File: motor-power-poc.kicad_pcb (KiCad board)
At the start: 4 copper layers, 70 x 50 mm, 159 parts, among them J1 Conn_01x04_Pin, J2 USB_C_Receptacle_USB2.0_14P, J3 Conn_01x02, J4 Conn_02x02_Counter_Clockwise, J5 Conn_02x06_Counter_Clockwise, M1 Motor_Servo, M2 Motor_Servo, M3 DC, Q1 Q_NMOS, Q10 Q_NMOS, Q2 Q_NMOS, Q3 Q_NMOS, Q4 Q_NMOS, Q5 Q_NMOS, Q6 Q_NMOS, Q7 Q_NMOS, Q8 Q_NMOS, Q9 Q_NMOS, SW1 SW_Push, SW2 SW_Push, U1 QRE1113GR, U10 CJ431, U11 DRV8701, U2 QRE1113GR, U3 QRE1113GR, U4 ESP32-S3FH4R2, U5 LM74502, U6 TPS5430DDA, U7 TPS56A37, U8 TPS2121, U9 LDL212PV33R, Y1 48M

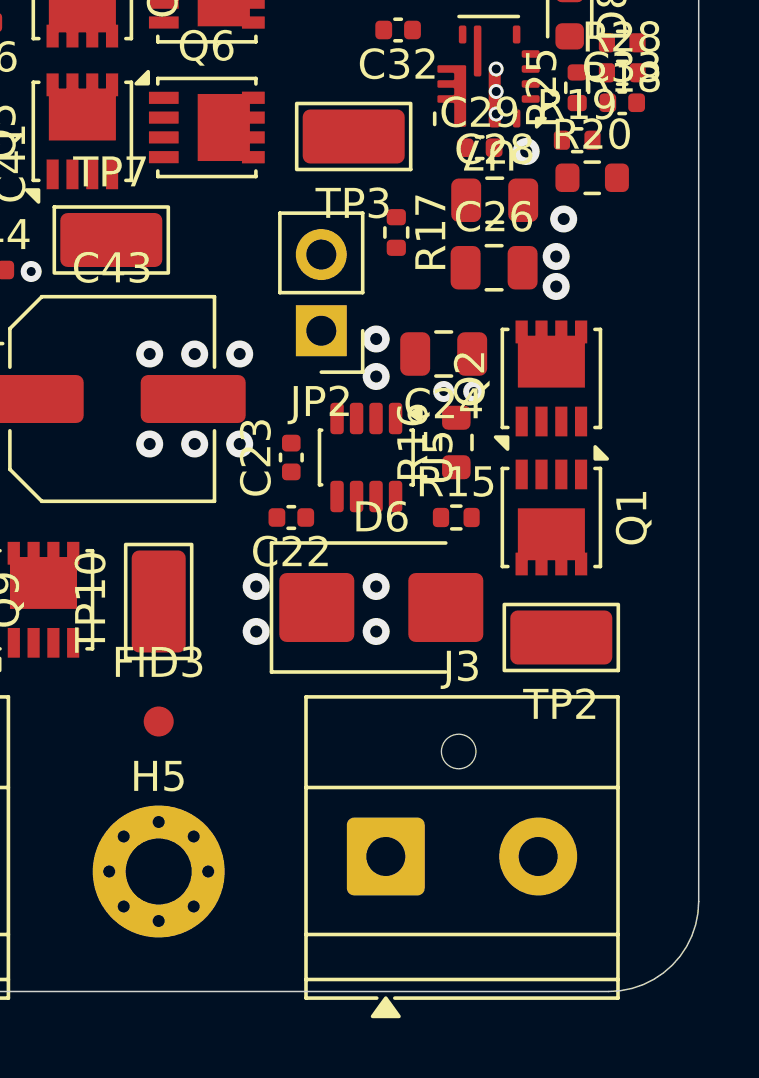
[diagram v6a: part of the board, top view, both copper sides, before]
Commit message: pcb: add LM74502H RPP routing
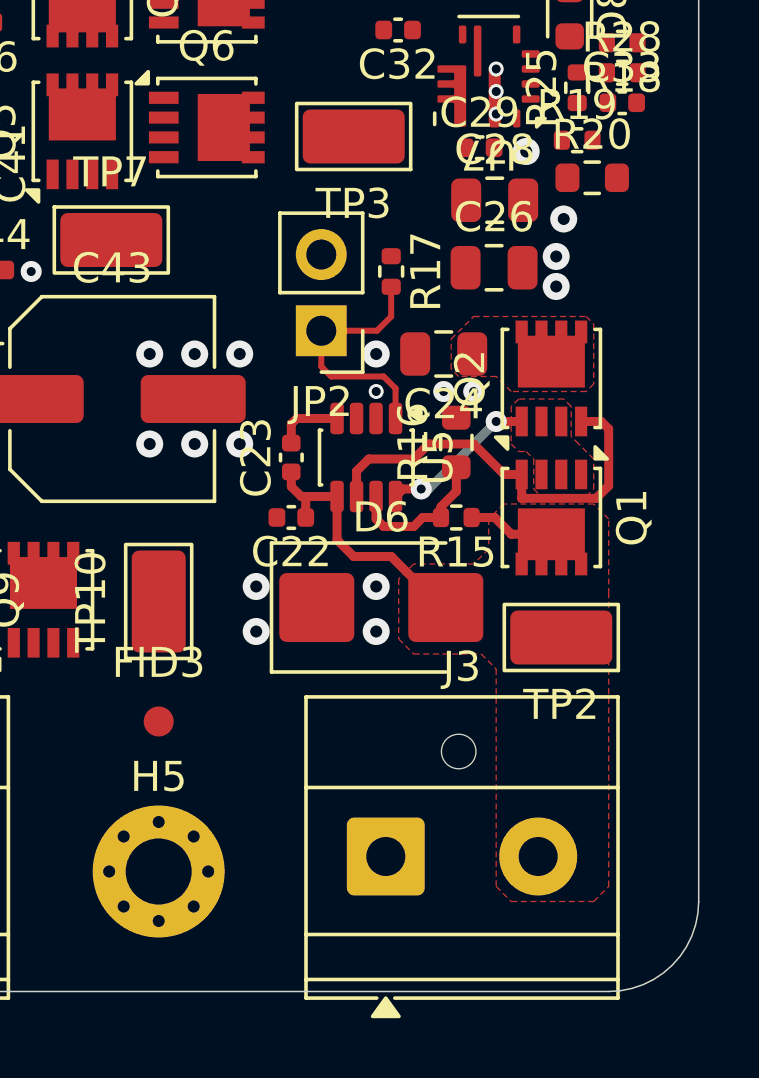
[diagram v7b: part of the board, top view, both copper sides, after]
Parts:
- moved R17 1.31 mm to (171.8, 80.0)
- turned R15 to 180 degrees
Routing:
- net Net-(Q1-G): track 0.00 -> 13.9 mm
- net /Connectors/EN/UVLO: track 0.00 -> 11.8 mm
- net Net-(JP2-A): track 0.00 -> 8.49 mm
- net Net-(U5-SRC): track 0.00 -> 5.24 mm, vias 0 -> 2
- net Net-(U5-OV): track 0.00 -> 5.03 mm
- net Net-(U5-VCAP): track 0.00 -> 2.24 mm
- added copper zone on F.Cu, net +Vin
- added copper zone on F.Cu, net /Connectors/EN/UVLO
- added copper zone on F.Cu, net Net-(U5-SRC)

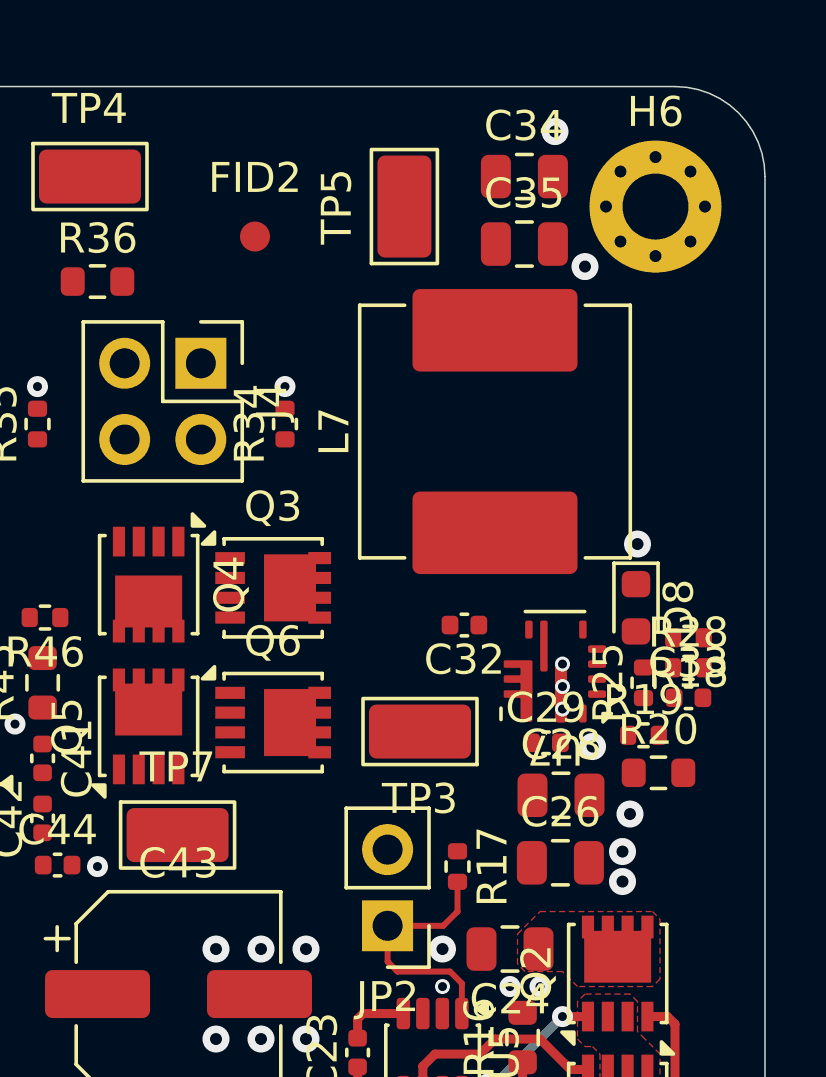
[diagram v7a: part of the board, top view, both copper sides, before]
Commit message: pcb: add TPS56A37 SMPS routing
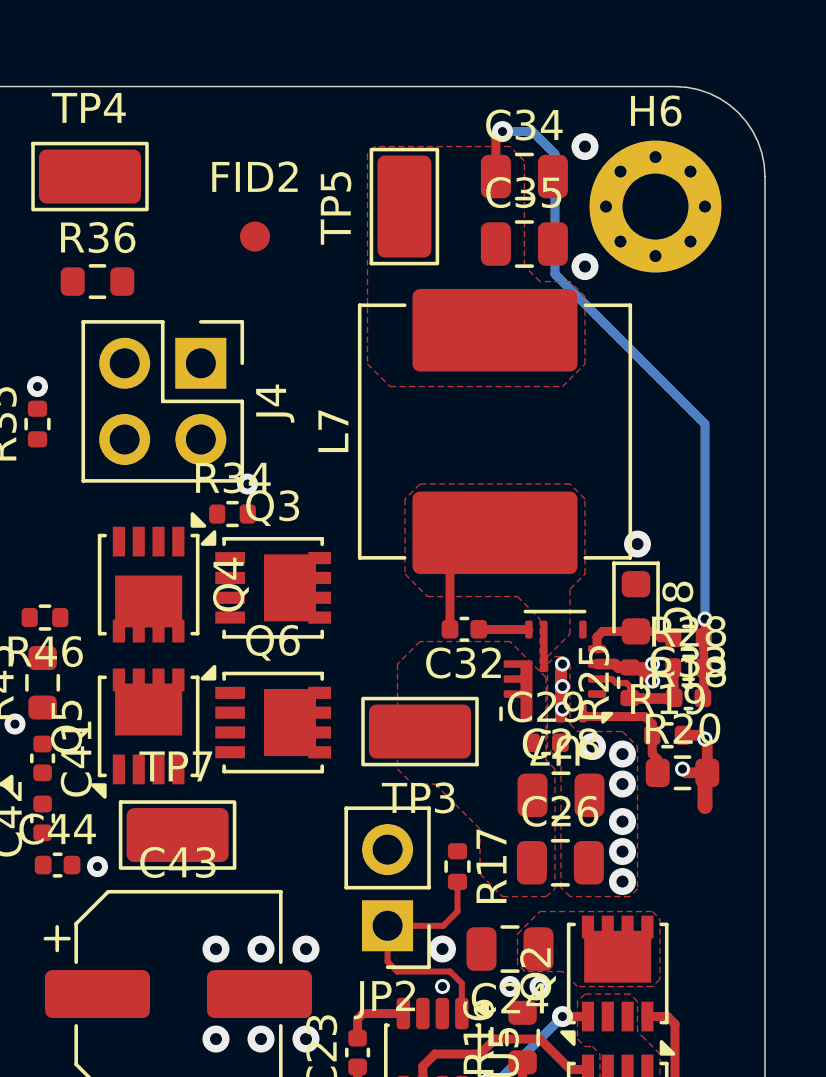
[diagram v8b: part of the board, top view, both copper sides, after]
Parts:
- added NT1: NetTie_2, NetTie:NetTie-2_SMD_Pad0.5mm, F.Cu at (180.0, 77.5)
- moved R34 3.47 mm to (164.2, 68.2), turned to 0 degrees
- moved R19 0.80 mm to (178.8, 75.6)
- moved R20 0.80 mm to (179.2, 76.9)
- moved R25 0.45 mm to (177.5, 73.9)
- moved C32 0.14 mm to (172.0, 72.1)
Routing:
- net +12V: track 0.00 -> 23.9 mm, vias 0 -> 2
- net AGND: track 0.00 -> 5.97 mm, vias 0 -> 4
- net Net-(U7-MODE): track 0.00 -> 4.16 mm
- net Net-(U7-FB): track 0.00 -> 4.09 mm
- net Net-(D8-A): track 0.00 -> 3.11 mm
- net Net-(U7-SW): track 0.00 -> 2.37 mm
- net Net-(U7-BOOT): track 0.00 -> 1.67 mm
- net GND: vias 114 -> 116
- added copper zone on F.Cu, net +12V
- added copper zone on In1.Cu, net AGND
- added copper zone on F.Cu, net GND
- added copper zone on F.Cu, net Net-(U7-SW)
